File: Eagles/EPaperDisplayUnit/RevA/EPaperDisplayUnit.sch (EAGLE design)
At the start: 100 parts, among them IC1 AT25, J26 SOLDER_JUMPER_2WAY-TRACE12, J27 SOLDER_JUMPER_2WAY-TRACE12, U2 LPC824M201JHI33, X1 32.768kHz, X2 FH12-50S-0.5SH

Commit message: [Draw schematic for the display unit #8]
use inch for Eagle ... don't like it but for fast turn round it needs to be done
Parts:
- removed D7: (no value), d:D-SCHOTTKY-SOD-123
- removed J26, J27: SOLDER_JUMPER_2WAY-TRACE12, rigado-connectors:SOLDER_JUMPER_2WAY-TRACE12
- removed JCUR: (no value), rigado-connectors:MA03-1SMT
- removed R20: 1R, r:R-0805
- removed TP11, TP12, TP4: TPSPAD1-13Y, testpad:TPSPAD1-13Y
- removed U1: (no value), BMD-200:BMD-200
- removed U4: (no value), rigado-power:VREG-SOT23
- removed X1: 32.768kHz, rigado-crystal:CRYSTAL2SMD
- added C35: 100nF, rcl:C-EUC0603
- added C36: 10uF, rcl:C-EUC0603
- added D4: BAT54, diode:BAT54
- added IC2: LT1763CS8-3.3, linear-technology:LT1763CS8-3.3
- added U$3: 90SMX, crystal:90SMX
- added U$6: EYAGJNZXXEYAGJNZXX, TAIYO-YUDEN:EYAGJNZXXEYAGJNZXX
- C1, C2: value 16p -> (none); device c:C-0402 -> adafruit:C-USC0603; DESCRIPTION CAP CER 16PF 50V 5% NP0 0402 -> (none); EACH 0.003 -> (none); MFPN CL05C160JB5NCNC -> (none); MFR Samsung -> (none); VEND Digikey -> (none); VPN 1276-1645-1-ND -> (none)
- C3: value 1uF -> 10uF; device c:C-0402 -> rcl:C-EUC0603; DESCRIPTION CAP CER 1UF 6.3V 5% X5R 0402 -> (none); EACH 0.006 -> (none); MFPN CL05A105JQ5NNNC -> (none); MFR Samsung -> (none); VEND Digikey -> (none); VPN 1276-1444-1-ND -> (none)
- C7: value 4.7u -> 100uF; device c:C-0603 -> rcl:C-EUC0603; DESCRIPTION CAP CER 4.7UF 6.3V 10% X5R 0603 -> (none); EACH 0.022 -> (none); MFPN GRM188R60J475KE19D -> (none); MFR Murata -> (none); VEND Digikey -> (none); VPN 490-3297-1-ND -> (none)
- C9: value 10uF -> 1uF; device c:C-0402 -> rcl:C-EUC0603; DESCRIPTION CAP CER 1UF 6.3V 5% X5R 0402 -> (none); EACH 0.006 -> (none); MFPN CL05A105JQ5NNNC -> (none); MFR Samsung -> (none); VEND Digikey -> (none); VPN 1276-1444-1-ND -> (none)
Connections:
- removed net 5V0: C6.1, LED1.A, U$23.1, U$8.VDD
- removed net N$3: J26.2, U1.P0.26
- removed net N$4: C7.1, JCUR.2, R20.2, U1.VCC
- removed net N$40: TP4.PP, U1.P0.11
- removed net P0.26: J26.3, TP11.PP
- removed net P0.27: J27.3, TP12.PP
- new net +3V3: C35.1, C7.1, TP8.PP, U$6.AVDD, U$6.VCC_NRF
- new net N$2: U$23.1
- new net N$41: IC2.SENSE
- new net N$44: U$6.OUT_ANT, U$6.OUT_MOD
- new net N$5: C6.1, LED1.A, U$8.VDD
- net !LED1: now also U$6.P0.21; no longer U1.P0.24
- net !LED2: now also U$6.P0.23; no longer U1.P0.25
- net !TCM_BUSY: now also U$6.P0.05; no longer U1.P0.05
- net !TCM_CS: now also U$6.P0.02; no longer U1.P0.02
- net !TCM_EN: now also U$6.P0.06; no longer U1.P0.06
- net BTN_BACKWARD: now also U$6.P0.19; no longer U1.P0.09
- net BTN_FORWARD: now also U$6.P0.17; no longer U1.P0.08
- net GND: now also C35.2, C7.2, IC2.BYP, IC2.GND@1, IC2.GND@2, IC2.GND@3, U$6.GND1, U$6.GND2, U$6.GND3, U$6.GND4, U$6.GND5, U$6.GND6; no longer C1.1, C2.1, C3.1, C7.3, C9.1, JCUR.3, U1.GND1, U1.GND10, U1.GND2, U1.GND3, U1.GND4, U1.GND5, U1.GND6, U1.GND7, U1.GND8, U1.GND9, U4.GND
- net N$1: now also U$6.P0.25; no longer U1.P0.00
- net N$19: now also U$6.P0.26/XL2; no longer C2.3, J27.1, X1.2
- net N$20: now also U$6.P0.27/XL1; no longer C1.3, J26.1, X1.1
- net N$23: now also Q3.S, R6.2; no longer J27.2, U1.P0.27
- net N$38: now also U$6.P0.00; no longer U1.P0.10
- net N$6: now also D4.A, IC2.OUT; no longer C9.3, D7.A, U4.OUT
- net SWCLK: now also U$6.SWDCLK; no longer U1.SWDCLK
- net SWDIO: now also U$6.SWDIO; no longer U1.SWDIO
- net TCM_MISO: now also U$6.P0.03; no longer U1.P0.03
- net TCM_MOSI: now also U$6.P0.01; no longer U1.P0.01
- net TCM_SCLK: now also U$6.P0.04; no longer U1.P0.04
- net VBATT: now also IC2.!SHDN, IC2.IN; no longer C3.3, U4.IN
- net VSYS: no longer D7.C, JCUR.1, Q3.S, R20.1, R6.2, TP8.PP
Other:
- note removed: "BMD-200 Module"
- note removed: "Current Sense for BMD-200"
- moved on the sheet: C6, D1, D2, LED1, LED2, LED3, R1, R2, R4, R5, S1, S2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

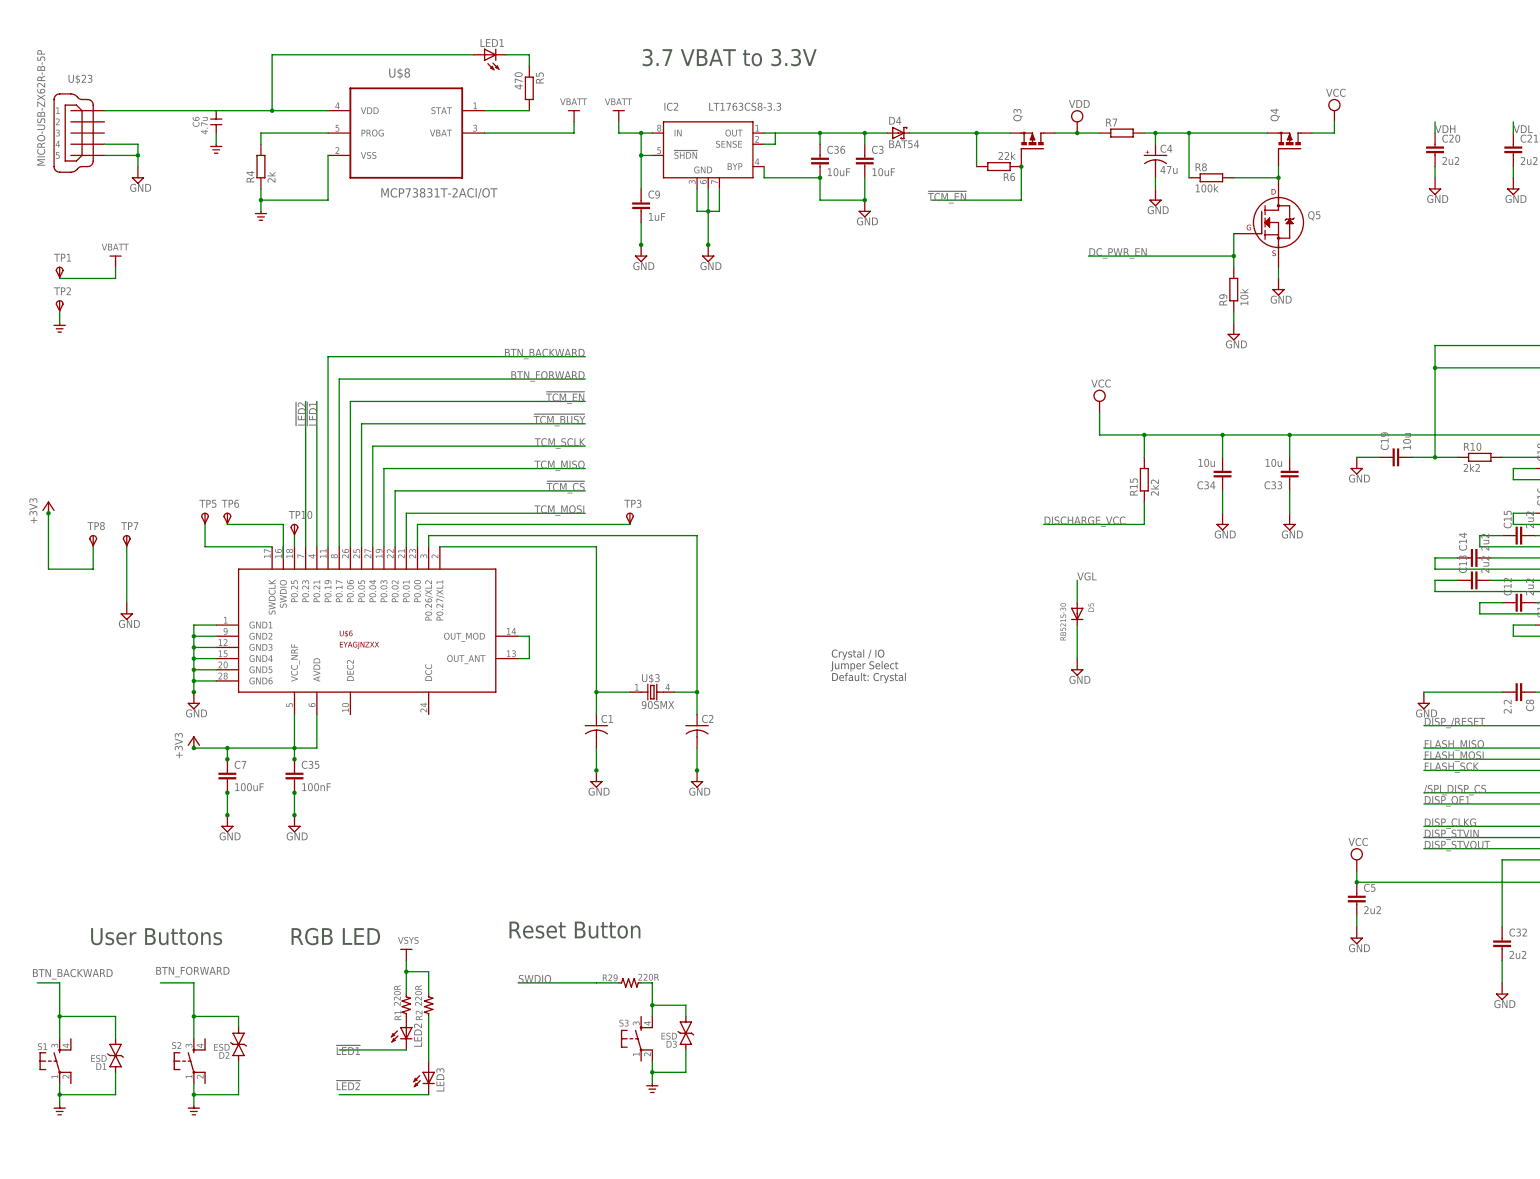
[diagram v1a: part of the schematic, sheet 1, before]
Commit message: [Draw schematic for the display unit #8]
committing final version of Rev A.

Need to visit the BOM later on.

Ok to proceed with PCB layout
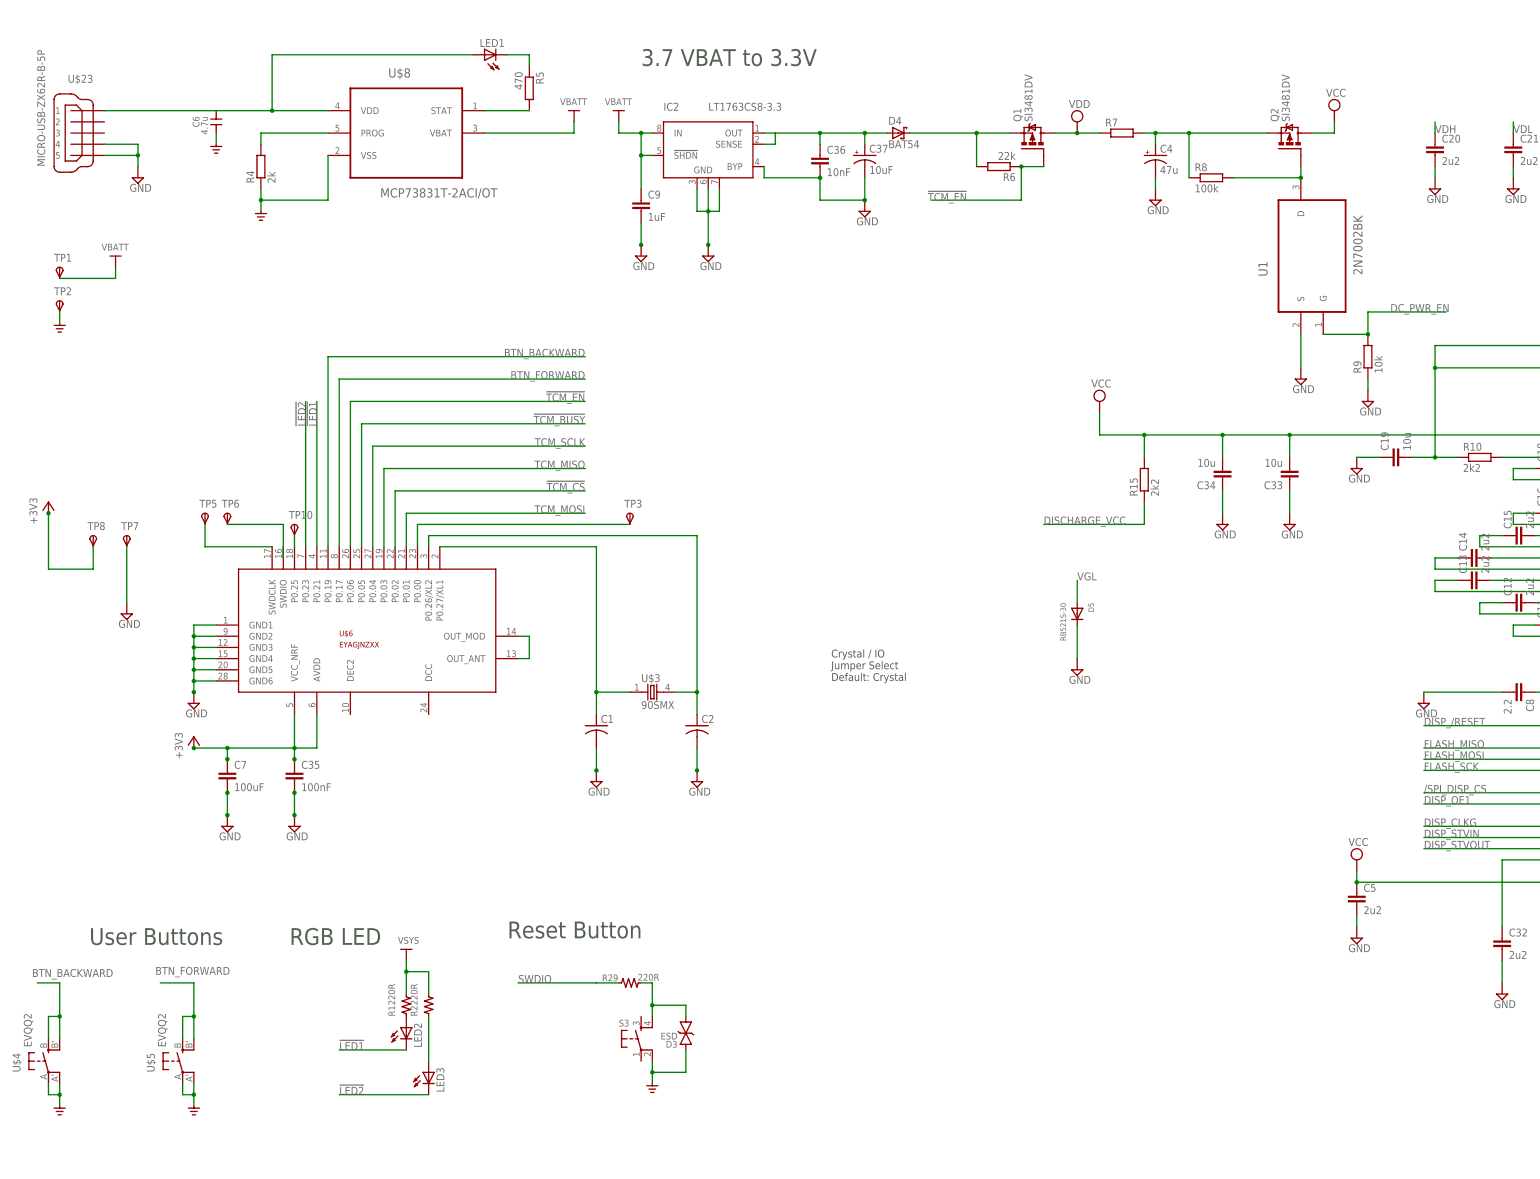
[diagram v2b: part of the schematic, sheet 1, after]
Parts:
- removed C3: 10uF, rcl:C-EUC0603
- removed D1, D2: ESD, d:ESDSOD-923
- removed Q3, Q4: (no value), transistor-power:NTR4171PTG
- removed Q5: (no value), transistors:2N7002_SOT23
- removed S1, S2: (no value), rigado-switches:10-XXTL3301-GW
- added C37: 10uF, adafruit:CPOL-US085CS-1AR
- added Q1, Q2: SI3481DV, transistor-power:SI3481DV
- added U$4, U$5: EVQQ2, adafruit:EVQQ2
- added U1: 2N7002BK, NXP_By_element14_Batch_1:2N7002BK
- C36: value 10uF -> 10nF
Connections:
- net !TCM_EN: now also Q1.G; no longer Q3.G
- net BTN_BACKWARD: now also U$4.S, U$4.S1; no longer D1.C, S1.S
- net BTN_FORWARD: now also U$5.S, U$5.S1; no longer D2.C, S2.S
- net DC_PWR_EN: now also U1.G; no longer Q5.G
- net GND: now also C37.-, U$4.P, U$4.P1, U$5.P, U$5.P1; no longer D1.A, D2.A, Q5.S, S1.P, S2.P
- net N$11: now also Q2.G, U1.D; no longer Q4.G, Q5.D
- net N$12: now also Q2.S; no longer Q4.S
- net N$23: now also Q1.S; no longer Q3.S
- net N$6: now also C37.+
- net VCC: now also Q2.D; no longer Q4.D
- net VDD: now also Q1.D; no longer Q3.D
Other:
- moved on the sheet: R9

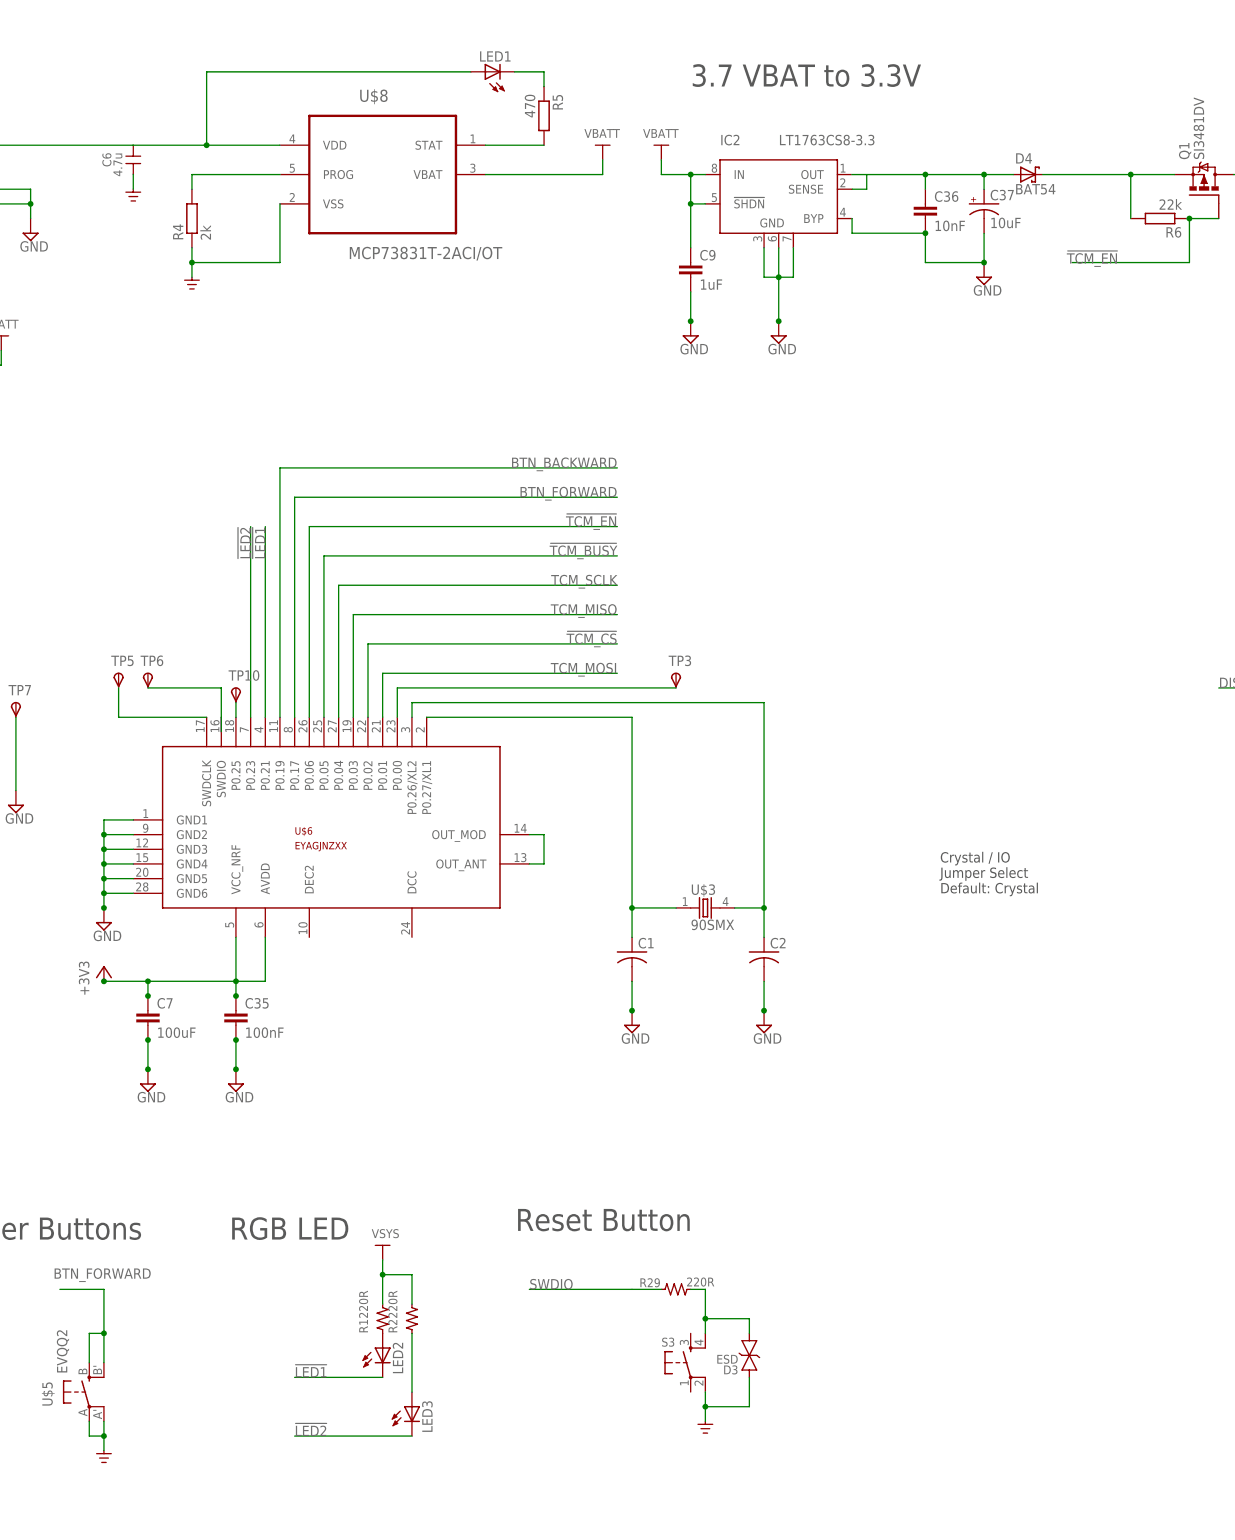
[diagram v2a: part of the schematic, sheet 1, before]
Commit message: [Draw schematic for the display unit #8]
minor changes to Rev A
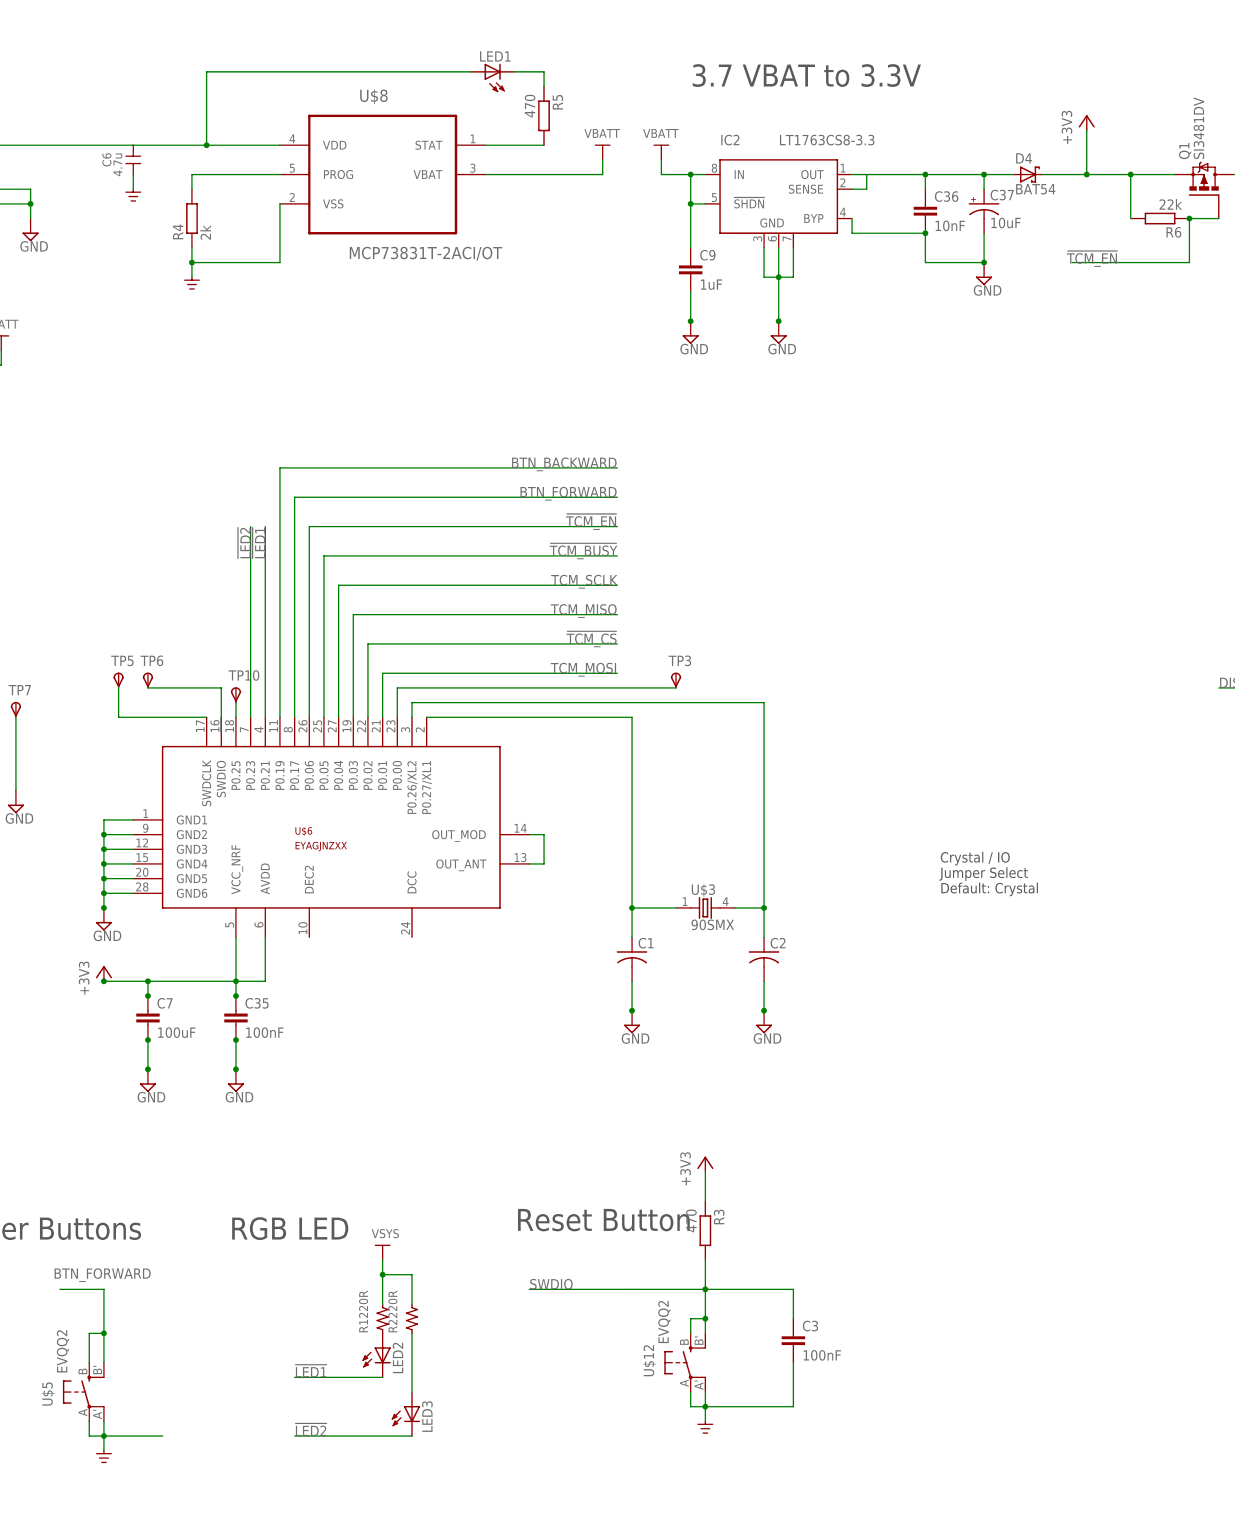
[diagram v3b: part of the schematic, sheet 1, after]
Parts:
- removed D3: ESD, d:ESDSOD-923
- removed R29: 220R, r:R-0402
- removed S3: (no value), rigado-switches:10-XXTL3301-GW
- added C3: 100nF, rcl:C-EUC0603
- added R3: 470, resistor:R-EU_R0402
- added U$12: EVQQ2, adafruit:EVQQ2
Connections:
- removed net N$23: Q1.S, R6.2
- removed net N$47: D3.C, R29.2, S3.S1
- net +3V3: now also Q1.S, R3.1, R6.2
- net GND: now also C3.2, U$12.P, U$12.P1; no longer D3.A, S3.P1
- net N$48: now also C3.1, R3.2, U$12.S, U$12.S1; no longer R29.1
